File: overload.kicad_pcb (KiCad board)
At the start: 2 copper layers, 100 x 100 mm, 26 parts, among them U1 NE5532

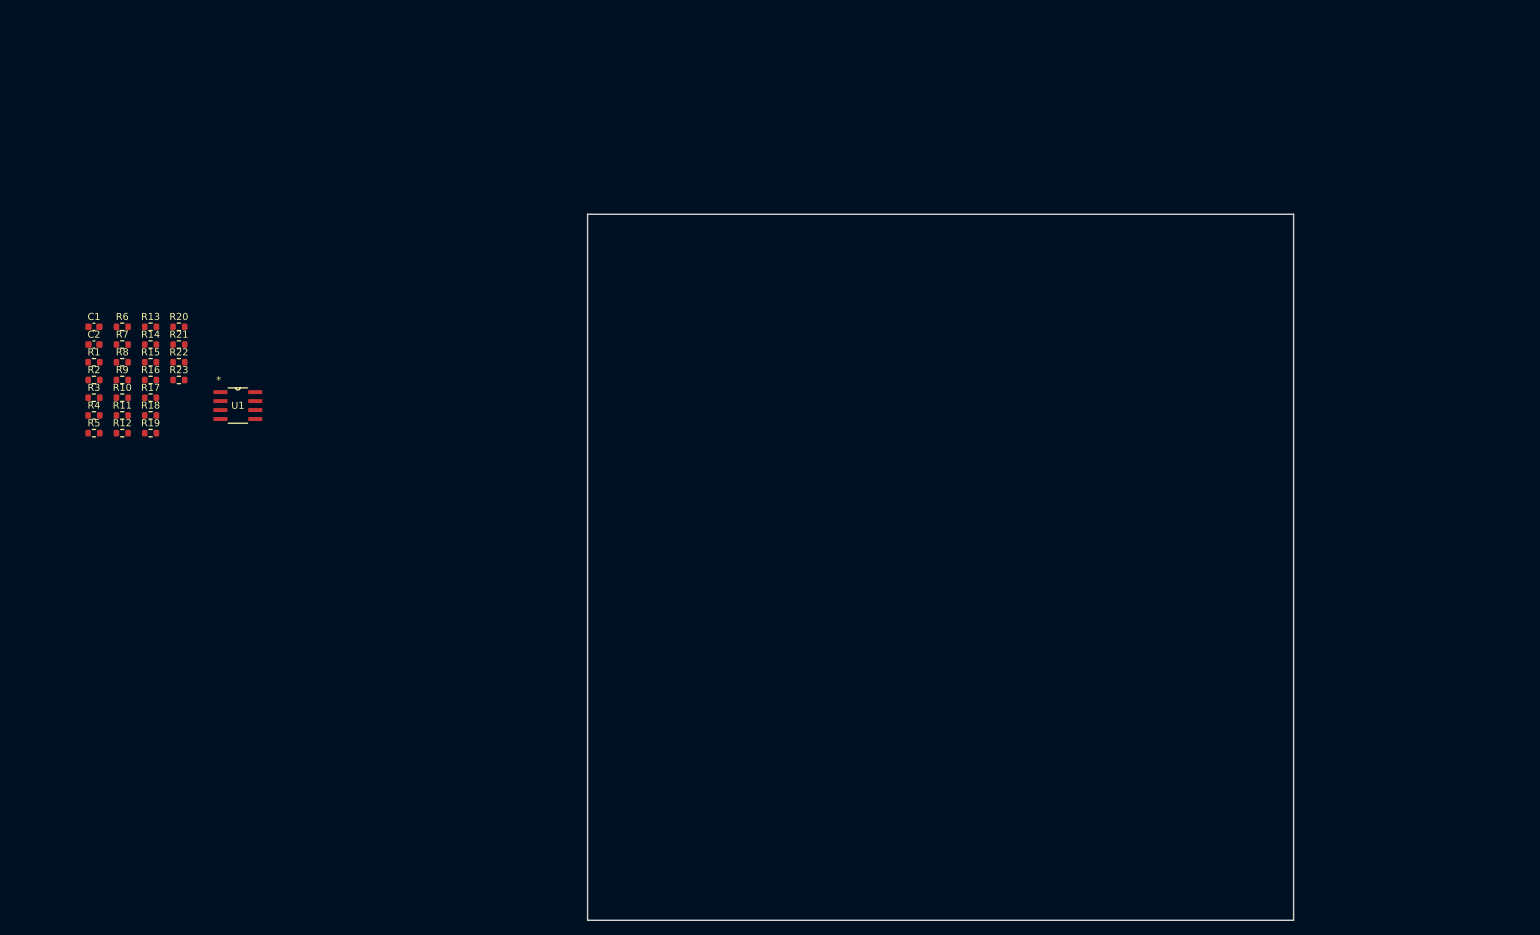
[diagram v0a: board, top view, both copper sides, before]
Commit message: initial component placement in pcb
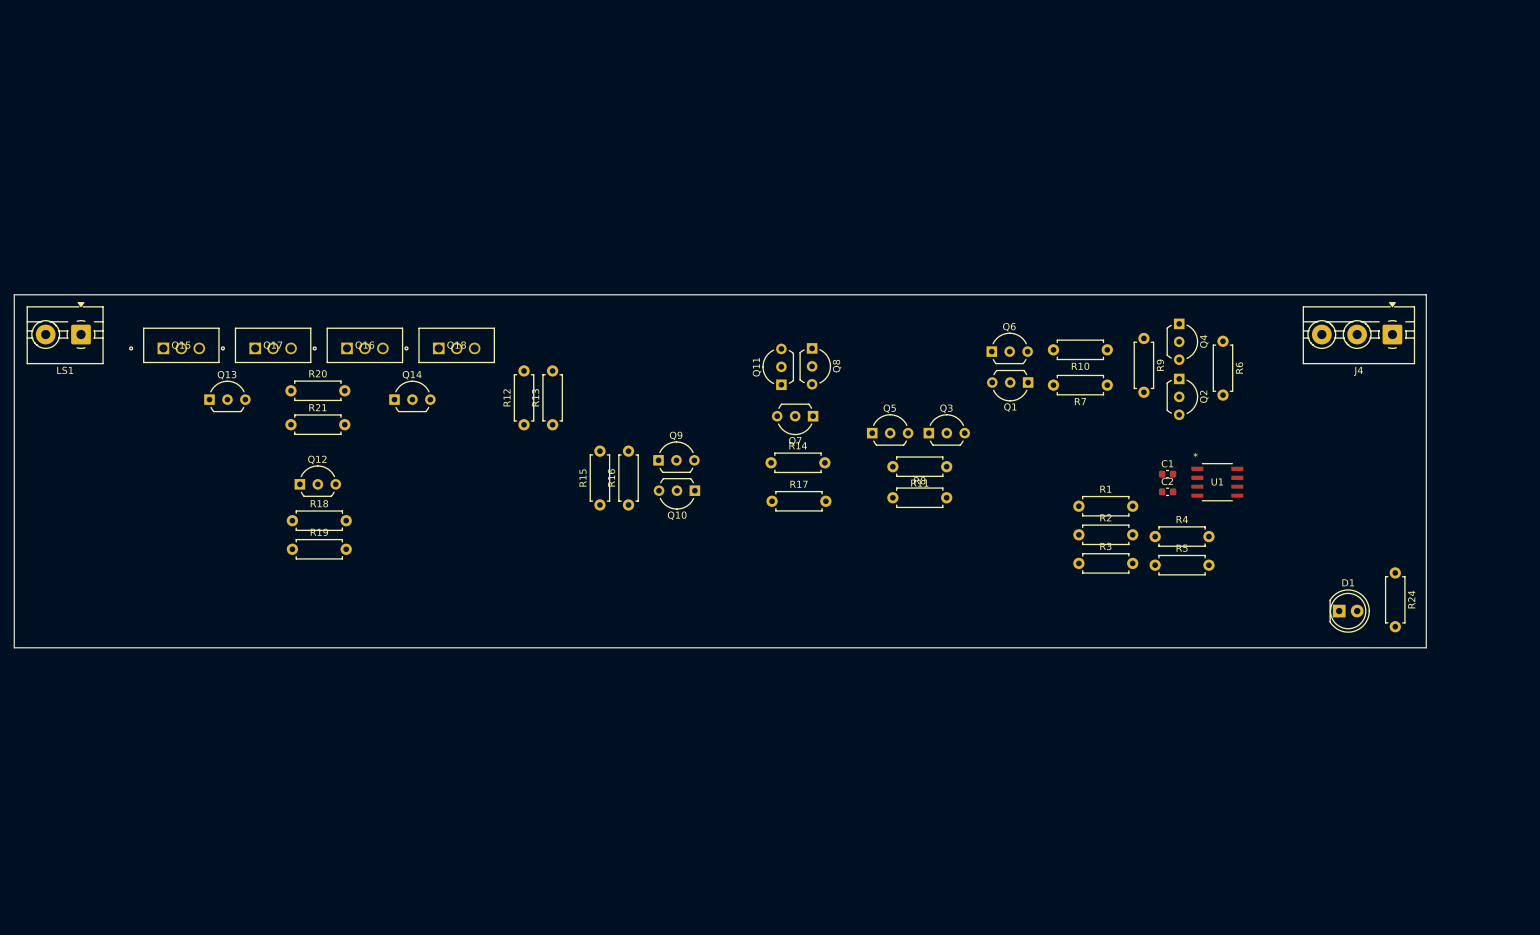
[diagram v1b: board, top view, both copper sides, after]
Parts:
- removed R22, R23: R, Resistor_SMD:R_0603_1608Metric
- added D1: LED, LED_THT:LED_D5.0mm, F.Cu at (239.5, 116.2)
- added J4: Conn_01x03, TerminalBlock:TerminalBlock_MaiXu_MX126-5.0-03P_1x03_P5.00mm, F.Cu at (247.0, 77.0)
- added LS1: Speaker, TerminalBlock:TerminalBlock_MaiXu_MX126-5.0-02P_1x02_P5.00mm, F.Cu at (61.2, 77.0)
- added Q1: PNP, 2N5401:P210_TO-92, F.Cu at (195.4, 83.8)
- added Q10: PNP, 2N5401:P210_TO-92, F.Cu at (148.2, 99.2)
- added Q11: NPN, 2N5401:P210_TO-92, F.Cu at (160.4, 84.2)
- added Q12: NPN, 2N5401:P210_TO-92, F.Cu at (92.2, 98.2)
- added Q13: NPN, 2N5401:P210_TO-92, F.Cu at (79.5, 86.2)
- added Q14: PNP, 2N5401:P210_TO-92, F.Cu at (105.7, 86.2)
- added Q15: NPN, D44H8:TO-220_STM, F.Cu at (72.9, 79.0)
- added Q16: PNP, D44H8:TO-220_STM, F.Cu at (98.9, 79.0)
- added Q17: NPN, D44H8:TO-220_STM, F.Cu at (85.9, 79.0)
- added Q18: PNP, D44H8:TO-220_STM, F.Cu at (111.9, 79.0)
- added Q2: PNP, 2N5401:P210_TO-92, F.Cu at (216.8, 83.3)
- added Q3: NPN, 2N5401:P210_TO-92, F.Cu at (181.3, 91.0)
- added Q4: PNP, 2N5401:P210_TO-92, F.Cu at (216.8, 75.5)
- added Q5: NPN, 2N5401:P210_TO-92, F.Cu at (173.3, 91.0)
- added Q6: PNP, 2N5401:P210_TO-92, F.Cu at (190.2, 79.5)
- added Q7: NPN, 2N5401:P210_TO-92, F.Cu at (164.9, 88.6)
- added Q8: NPN, 2N5401:P210_TO-92, F.Cu at (164.8, 79.0)
- added Q9: PNP, 2N5401:P210_TO-92, F.Cu at (143.1, 94.8)
- added R24: R, Resistor_THT:R_Axial_DIN0207_L6.3mm_D2.5mm_P7.62mm_Horizontal, F.Cu at (247.4, 110.8)
- R1, R10, R11, R12, R13, R14, R15, R16, R17, R18, R19, R2, R20, R21, R3, R4, R5, R6, R7, R8, R9: footprint Resistor_SMD:R_0603_1608Metric -> Resistor_THT:R_Axial_DIN0207_L6.3mm_D2.5mm_P7.62mm_Horizontal
- U1: footprint NE5532DR:D8 -> NE5532DR:D8-M
- moved R6 155.9 mm to (223.0, 78.0), turned to -90 degrees
- moved C1 153.5 mm to (215.1, 96.8)
- moved C2 153.5 mm to (215.1, 99.3)
- moved R5 151.5 mm to (213.4, 109.7)
- moved R4 151.3 mm to (213.4, 105.7)
- moved R9 144.8 mm to (211.8, 77.6), turned to -90 degrees
- moved R3 141.5 mm to (202.6, 109.5)
- moved R2 141.2 mm to (202.6, 105.4)
- moved R1 141.0 mm to (202.6, 101.3)
- moved R10 139.7 mm to (206.6, 79.2), turned to 180 degrees
- moved R7 139.6 mm to (206.6, 84.2), turned to 180 degrees
- moved U1 139.2 mm to (222.2, 98.0)
- moved R11 117.0 mm to (183.9, 95.8), turned to 180 degrees
- moved R8 110.8 mm to (176.2, 100.2)
- moved R14 89.5 mm to (159.0, 95.2)
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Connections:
- R1 pad 1: Net-(R1-Pad1) -> /Baxandall EQ/eq_in
- R1 pad 2: Net-(Q2-B) (its old number) -> Net-(C1-Pad1)
- R10 pad 1: Net-(Q4-E) -> Net-(Q4-C)
- R10 pad 2: -24V -> Net-(Q6-E)
- R12 pad 1: Net-(Q1-E) -> Net-(Q6-B)
- R12 pad 2: -24V -> GND
- R13 pad 1: Net-(Q8-B) -> Net-(Q6-B)
- R13 pad 2: -24V -> /Amplification/amp_out_fb
- R14 pad 1: Net-(Q10-B) (its old number) -> Net-(Q11-B)
- R14 pad 2: Net-(Q10-E) (its old number) -> -24V
- R15 pad 2: Net-(Q10-B) (its old number) -> GND
- R17 pad 2: GND -> -24V
- R18 pad 2: Net-(LS1-Pad1) -> Net-(Q12-B)
- R19 pad 1: Net-(LS1-Pad1) -> Net-(Q12-B)
- R2 pad 1: Net-(R2-Pad1) -> /Baxandall EQ/eq_in
- R20 pad 2: Net-(LS1-Pad1) -> /Amplification/amp_out_fb
- R21 pad 1: Net-(LS1-Pad1) -> /Amplification/amp_out_fb
- R3 pad 1: Net-(R2-Pad1) -> Net-(R3-Pad1)
- R3 pad 2: Net-(C1-Pad1) -> Net-(U1B--)
- R4 pad 2: Net-(Q2-B) (its old number) -> /Amplification/amp_in
- R5 pad 2: Net-(U1B--) -> /Amplification/amp_in
- R6 pad 1: +24V -> Net-(Q2-C)
- R6 pad 2: Net-(Q6-B) -> GND
- R7 pad 1: Net-(Q6-C) -> Net-(Q4-C)
- R7 pad 2: GND -> Net-(Q1-E)
- R8 pad 1: Net-(Q7-C) -> Net-(Q3-E)
- R8 pad 2: Net-(Q2-E) -> -24V
- R9 pad 1: Net-(Q7-C) -> +24V
- U1 pad 1: Net-(R2-Pad1) -> /Baxandall EQ/eq_in
- U1 pad 7: Net-(Q2-B) (its old number) -> /Amplification/amp_in
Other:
- board size 100 x 100 mm -> 200 x 50 mm

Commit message: feat: added potentiometes to pcb
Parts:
- added RV1: POT, Potentiometer_THT:Potentiometer_Alps_RK163_Single_Horizontal, F.Cu at (100.0, 134.0)
- added RV2: POT, Potentiometer_THT:Potentiometer_Alps_RK163_Single_Horizontal, F.Cu at (119.5, 134.0)
- added RV3: POT, Potentiometer_THT:Potentiometer_Alps_RK163_Single_Horizontal, F.Cu at (138.9, 134.0)
- added RV4: POT, Potentiometer_THT:Potentiometer_Alps_RK163_Single_Horizontal, F.Cu at (60.0, 133.9)
- added RV5: POT, Potentiometer_THT:Potentiometer_Alps_RK163_Single_Horizontal, F.Cu at (79.5, 133.9)

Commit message: initial routing
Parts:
- added J1: AudioPlug2, TRS625:TRS, F.Cu at (259.8, 45.7)
- moved J4 108.8 mm to (138.2, 77.0)
- moved RV3 20.5 mm to (150.4, 117.0)
- moved RV2 19.0 mm to (128.0, 117.0)
- moved R20 18.9 mm to (72.2, 87.4), turned to 180 degrees
- moved RV1 17.9 mm to (105.5, 117.0)
- moved RV5 17.3 mm to (83.0, 117.0)
- moved RV4 17.0 mm to (60.6, 117.0)
- moved R19 13.0 mm to (95.4, 95.2)
- moved R18 12.5 mm to (81.7, 95.2)
- moved R12 6.27 mm to (129.8, 87.4), turned to 0 degrees
- moved Q14 5.41 mm to (111.0, 87.3), turned to 180 degrees
- moved Q13 4.96 mm to (84.3, 87.3), turned to 180 degrees
- moved Q12 4.00 mm to (89.8, 101.5)
- moved R13 3.43 mm to (125.6, 87.4), turned to 180 degrees
- moved R21 2.41 mm to (91.3, 87.4)
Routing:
- net /Amplification/amp_out_fb: track 0.00 -> 108.6 mm
- net +24V: track 0.00 -> 99.5 mm
- net -24V: track 0.00 -> 49.4 mm
- net Net-(Q11-C): track 0.00 -> 20.8 mm
- net Net-(Q10-C): track 0.00 -> 18.5 mm
- net Net-(Q13-E): track 0.00 -> 15.0 mm
- net Net-(Q14-E): track 0.00 -> 15.0 mm
- net Net-(Q12-B): track 0.00 -> 12.3 mm
- net Net-(Q6-B): track 0.00 -> 4.18 mm

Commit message: hell yea, angelo do your magic
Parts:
- moved J1 74.3 mm to (225.2, 111.4)
- moved C1 43.8 mm to (227.1, 54.7)
- moved R2 43.8 mm to (214.6, 63.2)
- moved R3 43.8 mm to (214.6, 67.3)
- moved R4 43.8 mm to (225.4, 63.5)
- moved R5 43.8 mm to (225.4, 67.5)
- moved U1 43.8 mm to (234.2, 55.8)
- moved C2 43.8 mm to (227.1, 57.2)
- moved R1 43.8 mm to (214.6, 59.2)
- moved R15 11.7 mm to (124.8, 95.0), turned to 0 degrees
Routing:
- net Net-(Q10-C): track 18.5 -> 0.00 mm
- net Net-(Q12-B): track 12.3 -> 3.00 mm
- net /Amplification/amp_out_fb: track 108.6 -> 99.8 mm
- net Net-(Q6-B): track 4.18 -> 0.00 mm
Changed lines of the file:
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@@
 	(footprint "Resistor_THT:R_Axial_DIN0207_L6.3mm_D2.5mm_P7.62mm_Horizontal"
 		(layer "F.Cu")
-		(at 202.59 101.35)
+		(at 214.59 59.2)
 		(descr "Resistor, Axial_DIN0207 series, Axial, Horizontal, pin pitch=7.62mm, 0.25W = 1/4W, length*diameter=6.3*2.5mm^2, http://cdn-reichelt.de/documents/datenblatt/B400/1_4W%23YAG.pdf")
 		(tags "Resistor Axial_DIN0207 series Axial Horizontal pin pitch 7.62mm 0.25W = 1/4W length 6.3mm diameter 2.5mm")
@@
 	(footprint "TRS625:TRS"
 		(layer "F.Cu")
-		(at 259.8 45.7)
+		(at 225.2 111.4)
 		(property "Reference" "J1"
 			(at -3.5 0 90)
@@
 	(footprint "Resistor_THT:R_Axial_DIN0207_L6.3mm_D2.5mm_P7.62mm_Horizontal"
 		(layer "F.Cu")
-		(at 202.59 105.4)
+		(at 214.59 63.25)
 		(descr "Resistor, Axial_DIN0207 series, Axial, Horizontal, pin pitch=7.62mm, 0.25W = 1/4W, length*diameter=6.3*2.5mm^2, http://cdn-reichelt.de/documents/datenblatt/B400/1_4W%23YAG.pdf")
 		(tags "Resistor Axial_DIN0207 series Axial Horizontal pin pitch 7.62mm 0.25W = 1/4W length 6.3mm diameter 2.5mm")
@@
 	(footprint "Capacitor_SMD:C_0603_1608Metric"
 		(layer "F.Cu")
-		(at 215.14925 96.805)
+		(at 227.14925 54.655)
 		(descr "Capacitor SMD 0603 (1608 Metric), square (rectangular) end terminal, IPC_7351 nominal, (Body size source: IPC-SM-782 page 76, https://www.pcb-3d.com/wordpress/wp-content/uploads/ipc-sm-782a_amendment_1_and_2.pdf), generated with kicad-footprint-generator")
 		(tags "capacitor")
@@
 	(footprint "Capacitor_SMD:C_0603_1608Metric"
 		(layer "F.Cu")
-		(at 215.14925 99.315)
+		(at 227.14925 57.165)
 		(descr "Capacitor SMD 0603 (1608 Metric), square (rectangular) end terminal, IPC_7351 nominal, (Body size source: IPC-SM-782 page 76, https://www.pcb-3d.com/wordpress/wp-content/uploads/ipc-sm-782a_amendment_1_and_2.pdf), generated with kicad-footprint-generator")
 		(tags "capacitor")
@@
 	(footprint "Resistor_THT:R_Axial_DIN0207_L6.3mm_D2.5mm_P7.62mm_Horizontal"
 		(layer "F.Cu")
-		(at 213.39 105.65)
+		(at 225.39 63.5)
 		(descr "Resistor, Axial_DIN0207 series, Axial, Horizontal, pin pitch=7.62mm, 0.25W = 1/4W, length*diameter=6.3*2.5mm^2, http://cdn-reichelt.de/documents/datenblatt/B400/1_4W%23YAG.pdf")
 		(tags "Resistor Axial_DIN0207 series Axial Horizontal pin pitch 7.62mm 0.25W = 1/4W length 6.3mm diameter 2.5mm")
@@
 	(footprint "Resistor_THT:R_Axial_DIN0207_L6.3mm_D2.5mm_P7.62mm_Horizontal"
 		(layer "F.Cu")
-		(at 202.59 109.45)
+		(at 214.59 67.3)
 		(descr "Resistor, Axial_DIN0207 series, Axial, Horizontal, pin pitch=7.62mm, 0.25W = 1/4W, length*diameter=6.3*2.5mm^2, http://cdn-reichelt.de/documents/datenblatt/B400/1_4W%23YAG.pdf")
 		(tags "Resistor Axial_DIN0207 series Axial Horizontal pin pitch 7.62mm 0.25W = 1/4W length 6.3mm diameter 2.5mm")
@@
 	(footprint "NE5532DR:D8-M"
 		(layer "F.Cu")
-		(at 222.2 97.95)
+		(at 234.2 55.8)
 		(tags "NE5532DR ")
 		(property "Reference" "U1"
@@
 	(footprint "Resistor_THT:R_Axial_DIN0207_L6.3mm_D2.5mm_P7.62mm_Horizontal"
 		(layer "F.Cu")
-		(at 213.39 109.7)
+		(at 225.39 67.55)
 		(descr "Resistor, Axial_DIN0207 series, Axial, Horizontal, pin pitch=7.62mm, 0.25W = 1/4W, length*diameter=6.3*2.5mm^2, http://cdn-reichelt.de/documents/datenblatt/B400/1_4W%23YAG.pdf")
 		(tags "Resistor Axial_DIN0207 series Axial Horizontal pin pitch 7.62mm 0.25W = 1/4W length 6.3mm diameter 2.5mm")
@@
 	(footprint "Resistor_THT:R_Axial_DIN0207_L6.3mm_D2.5mm_P7.62mm_Horizontal"
 		(layer "F.Cu")
-		(at 134.75 101.17 90)
+		(at 124.8 95)
 		(descr "Resistor, Axial_DIN0207 series, Axial, Horizontal, pin pitch=7.62mm, 0.25W = 1/4W, length*diameter=6.3*2.5mm^2, http://cdn-reichelt.de/documents/datenblatt/B400/1_4W%23YAG.pdf")
 		(tags "Resistor Axial_DIN0207 series Axial Horizontal pin pitch 7.62mm 0.25W = 1/4W length 6.3mm diameter 2.5mm")
 		(property "Reference" "R15"
-			(at 3.81 -2.37 90)
+			(at 3.81 -2.37 360)
 			(layer "F.SilkS")
 			(effects
@@
 		)
 		(property "Value" "R"
-			(at 3.81 2.37 90)
+			(at 3.81 2.37 360)
 			(layer "F.Fab")
 			(effects
@@
 		)
 		(property "Footprint" "Resistor_THT:R_Axial_DIN0207_L6.3mm_D2.5mm_P7.62mm_Horizontal"
-			(at 0 0 90)
+			(at 0 0 0)
 			(unlocked yes)
 			(layer "F.Fab")
@@
 		)
 		(property "Datasheet" ""
-			(at 0 0 90)
+			(at 0 0 0)
 			(unlocked yes)
 			(layer "F.Fab")
@@
 		)
 		(property "Description" "Resistor"
-			(at 0 0 90)
+			(at 0 0 0)
 			(unlocked yes)
 			(layer "F.Fab")
@@
 		(attr through_hole)
 		(fp_line
-			(start 7.08 -1.37)
-			(end 7.08 -1.04)
+			(start 0.54 -1.37)
+			(end 7.08 -1.37)
 			(stroke
 				(width 0.12)
@@
 		)
 		(fp_line
-			(start 0.54 -1.37)
-			(end 7.08 -1.37)
+			(start 0.54 -1.04)
+			(end 0.54 -1.37)
 			(stroke
 				(width 0.12)
@@
 		)
 		(fp_line
-			(start 0.54 -1.04)
-			(end 0.54 -1.37)
+			(start 0.54 1.04)
+			(end 0.54 1.37)
 			(stroke
 				(width 0.12)
@@
 		)
 		(fp_line
-			(start 0.54 1.04)
-			(end 0.54 1.37)
+			(start 0.54 1.37)
+			(end 7.08 1.37)
 			(stroke
 				(width 0.12)
@@
 		)
 		(fp_line
-			(start 7.08 1.37)
-			(end 7.08 1.04)
+			(start 7.08 -1.37)
+			(end 7.08 -1.04)
 			(stroke
 				(width 0.12)
@@
 		)
 		(fp_line
-			(start 0.54 1.37)
-			(end 7.08 1.37)
+			(start 7.08 1.37)
+			(end 7.08 1.04)
 			(stroke
 				(width 0.12)
@@
 		)
 		(fp_line
-			(start 8.67 -1.5)
-			(end -1.05 -1.5)
+			(start -1.05 -1.5)
+			(end -1.05 1.5)
 			(stroke
 				(width 0.05)
@@
 		)
 		(fp_line
-			(start -1.05 -1.5)
-			(end -1.05 1.5)
+			(start -1.05 1.5)
+			(end 8.67 1.5)
 			(stroke
 				(width 0.05)
@@
 		)
 		(fp_line
-			(start 8.67 1.5)
-			(end 8.67 -1.5)
+			(start 8.67 -1.5)
+			(end -1.05 -1.5)
 			(stroke
 				(width 0.05)
@@
 		)
 		(fp_line
-			(start -1.05 1.5)
-			(end 8.67 1.5)
+			(start 8.67 1.5)
+			(end 8.67 -1.5)
 			(stroke
 				(width 0.05)
@@
 		)
 		(fp_line
-			(start 6.96 -1.25)
-			(end 0.66 -1.25)
+			(start 0 0)
+			(end 0.66 0)
 			(stroke
 				(width 0.1)
@@
 		)
 		(fp_line
-			(start 7.62 0)
-			(end 6.96 0)
+			(start 0.66 1.25)
+			(end 6.96 1.25)
 			(stroke
 				(width 0.1)
@@
 		)
 		(fp_line
-			(start 0 0)
-			(end 0.66 0)
+			(start 6.96 -1.25)
+			(end 0.66 -1.25)
 			(stroke
 				(width 0.1)
@@
 		)
 		(fp_line
-			(start 0.66 1.25)
-			(end 6.96 1.25)
+			(start 7.62 0)
+			(end 6.96 0)
 			(stroke
 				(width 0.1)
@@
 		)
 		(fp_text user "${REFERENCE}"
-			(at 3.81 0 90)
+			(at 3.81 0 360)
 			(layer "F.Fab")
 			(effects
@@
 		)
 		(pad "1" thru_hole circle
-			(at 0 0 90)
+			(at 0 0)
 			(size 1.6 1.6)
 			(drill 0.8)
@@
 		)
 		(pad "2" thru_hole oval
-			(at 7.62 0 90)
+			(at 7.62 0)
 			(size 1.6 1.6)
 			(drill 0.8)
@@
 	)
 	(segment
-		(start 129.79 87.4)
-		(end 125.61 87.4)
-		(width 1.5)
-		(layer "F.Cu")
-		(net 9)
-	)
-	(segment
 		(start 84.45 87.35)
 		(end 85.92 85.88)
@@
 	)
 	(segment
-		(start 87.993333 101.45)
-		(end 81.743333 95.2)
-		(width 1.5)
-		(layer "F.Cu")
-		(net 17)
-	)
-	(segment
-		(start 81.743333 95.2)
-		(end 81.743333 87.35)
-		(width 1.5)
-		(layer "F.Cu")
-		(net 17)
-	)
-	(segment
-		(start 89.85 101.45)
-		(end 87.993333 101.45)
-		(width 1.5)
-		(layer "F.Cu")
-		(net 17)
-	)
-	(segment
 		(start 108.41 89.81)
 		(end 103.02 95.2)
@@
 	)
 	(segment
-		(start 117.99 87.4)
-		(end 117 86.41)
-		(width 1.5)
-		(layer "F.Cu")
-		(net 27)
-	)
-	(segment
 		(start 64.59 80.3725)
 		(end 61.25 77.0325)
@@
 	)
 	(segment
-		(start 117 86.41)
-		(end 117 79)
-		(width 1.5)
-		(layer "F.Cu")
-		(net 27)
-	)
-	(segment
 		(start 91.256666 79.256666)
 		(end 91 79)
@@
 	)
 	(segment
-		(start 92.39 95.21)
-		(end 92.4 95.2)
-		(width 1.5)
-		(layer "F.Cu")
-		(net 29)
-	)
-	(segment
-		(start 92.39 101.45)
-		(end 92.39 95.21)
-		(width 1.5)
-		(layer "F.Cu")
-		(net 29)
-	)
-	(segment
-		(start 92.4 95.2)
-		(end 89.363333 95.2)
-		(width 1.5)
-		(layer "F.Cu")
-		(net 29)
-	)
-	(segment

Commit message: route bjt amplifier stage
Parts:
- removed C1, C2: C, Capacitor_SMD:C_0603_1608Metric
- moved J4 108.8 mm to (247.0, 77.2)
- moved R6 36.9 mm to (186.2, 80.6)
- moved U1 35.8 mm to (220.4, 88.8), turned to 90 degrees
- moved Q17 31.3 mm to (117.2, 78.2), turned to 180 degrees
- moved Q2 27.4 mm to (189.5, 82.2), turned to 0 degrees
- moved Q8 26.5 mm to (145.9, 97.6), turned to 180 degrees
- moved Q4 24.9 mm to (194.6, 86.6), turned to 180 degrees
- moved Q16 22.2 mm to (76.7, 78.2), turned to 180 degrees
- moved Q11 21.7 mm to (140.8, 93.2), turned to 0 degrees
- moved R14 20.7 mm to (140.7, 85.4)
- moved R16 20.2 mm to (120.8, 92.0), turned to -90 degrees
- moved Q14 19.5 mm to (91.5, 86.5), turned to -90 degrees
- moved R10 18.8 mm to (193.8, 92.9)
- moved R7 18.8 mm to (193.8, 97.9)
- moved Q1 18.8 mm to (182.6, 97.5)
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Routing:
- net -24V: track 49.4 -> 197.1 mm
- net +24V: track 99.5 -> 207.6 mm
- net Net-(Q6-B): track 0.00 -> 72.5 mm, vias 0 -> 1
- net Net-(Q10-C): track 0.00 -> 64.7 mm
- net Net-(Q11-C): track 20.8 -> 72.1 mm
- net Net-(Q14-E): track 15.0 -> 65.3 mm, vias 0 -> 2
- net Net-(Q13-E): track 15.0 -> 62.9 mm
- net Net-(Q1-C): track 0.00 -> 34.7 mm
- net Net-(Q12-B): track 3.00 -> 35.9 mm
- net Net-(Q3-B): track 0.00 -> 25.1 mm
- net Net-(Q11-B): track 0.00 -> 14.5 mm
- net Net-(Q2-B): track 0.00 -> 13.6 mm
- net Net-(Q10-B): track 0.00 -> 12.9 mm
- net Net-(Q1-E): track 0.00 -> 11.9 mm
- net Net-(Q4-C): track 0.00 -> 11.6 mm
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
